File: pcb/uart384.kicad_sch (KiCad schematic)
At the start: 33 parts, among them IC1 ICE40LP384-SG32, J1 USB_A, J2 TC2050, J3 Conn_02x06_Odd_Even, SW1 SW_Push, U1 CP2102-QFN28, U2 AT25DF256-SSHN, U3 MIC5365-1.2YC5, Y1 XO32

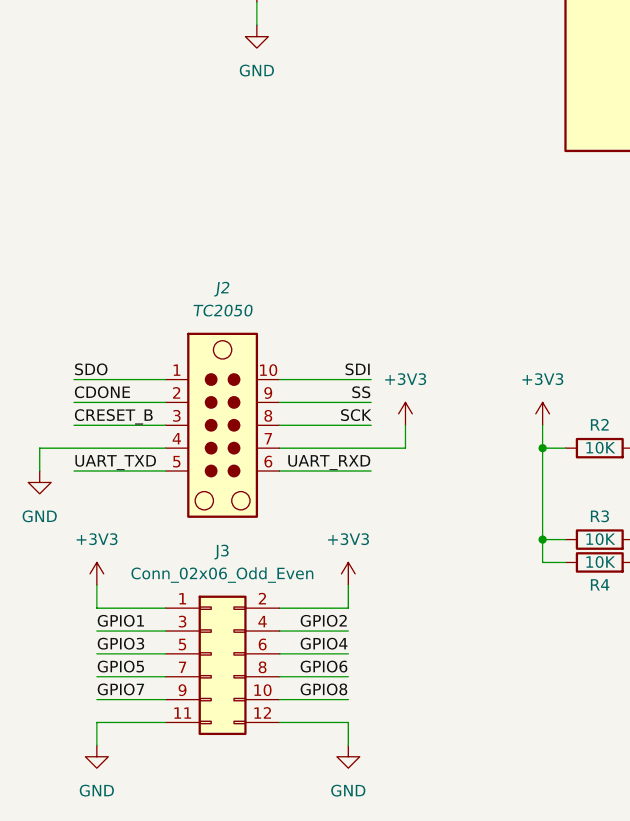
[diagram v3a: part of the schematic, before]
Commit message: PCB: add 5V to pinheader, move switch, LED, some resistors, improve routing
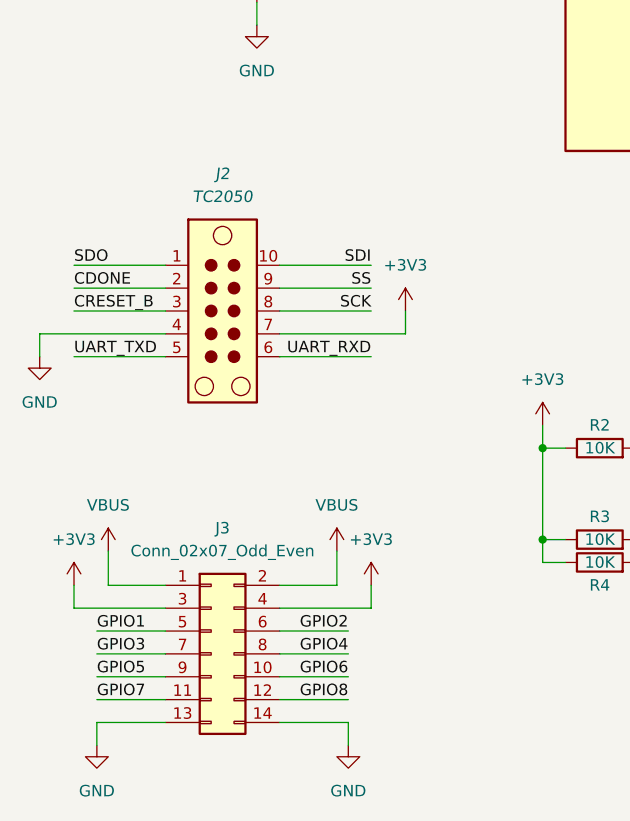
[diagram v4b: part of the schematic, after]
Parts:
- removed J3: Conn_02x06_Odd_Even, Connector_PinHeader_2.54mm:PinHeader_2x06_P2.54mm_Vertical, symbol Connector_Generic:Conn_02x06_Odd_Even
- added J3: Conn_02x07_Odd_Even, Connector_PinHeader_2.54mm:PinHeader_2x07_P2.54mm_Vertical, symbol Connector_Generic:Conn_02x07_Odd_Even
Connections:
- net +3V3: now also J3.3 (Pin_3), J3.4 (Pin_4)
- net GND: now also J3.13 (Pin_13), J3.14 (Pin_14)
- net GPIO1: now also J3.5 (Pin_5)
- net GPIO2: now also J3.6 (Pin_6)
- net GPIO3: now also J3.7 (Pin_7)
- net GPIO4: now also J3.8 (Pin_8)
- net GPIO5: now also J3.9 (Pin_9)
- net GPIO6: now also J3.10 (Pin_10)
- net GPIO7: now also J3.11 (Pin_11)
- net GPIO8: now also J3.12 (Pin_12)
- net VBUS: now also J3.1 (Pin_1), J3.2 (Pin_2)
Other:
- moved on the sheet: J2

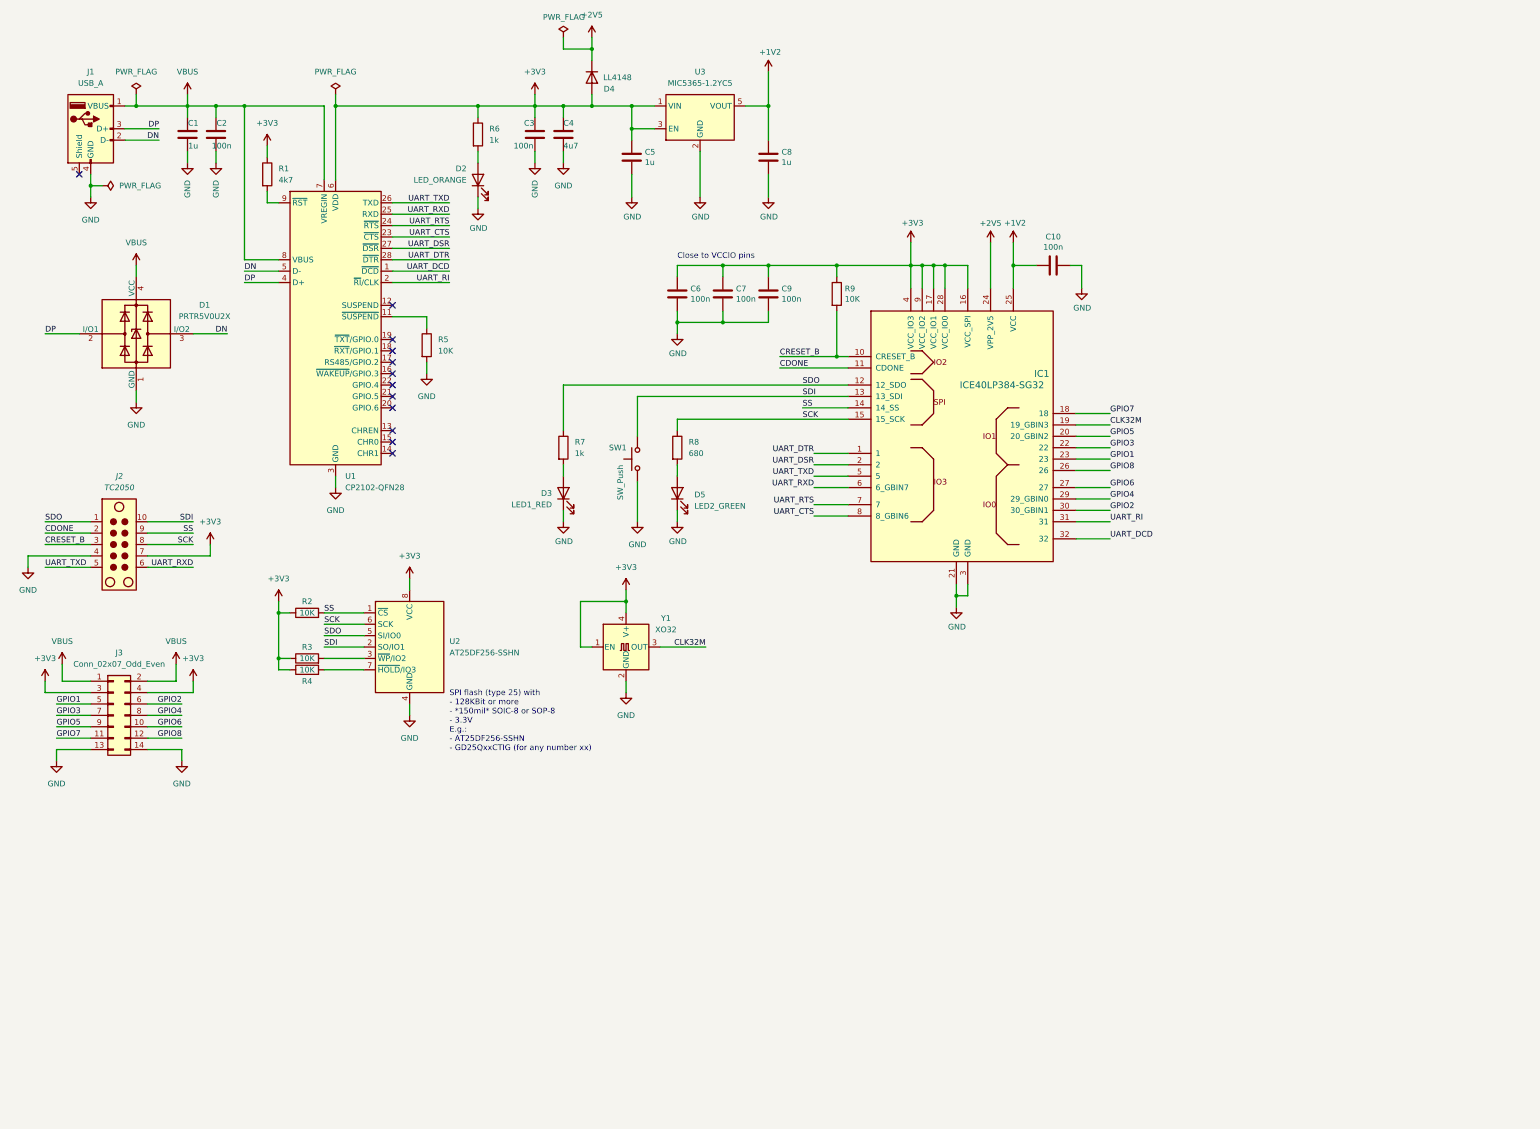
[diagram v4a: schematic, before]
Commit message: PCB: add additional header for upstream TC2050, re-route PCB.
Adding J4 for the "other" side of a TC2050 cable allows programming a
UART384 with another UART384, once a gateware is written that also can
control CDONE and CRESET lines. This enables full bootstrapping of a
UART384 with a UART384 :-D
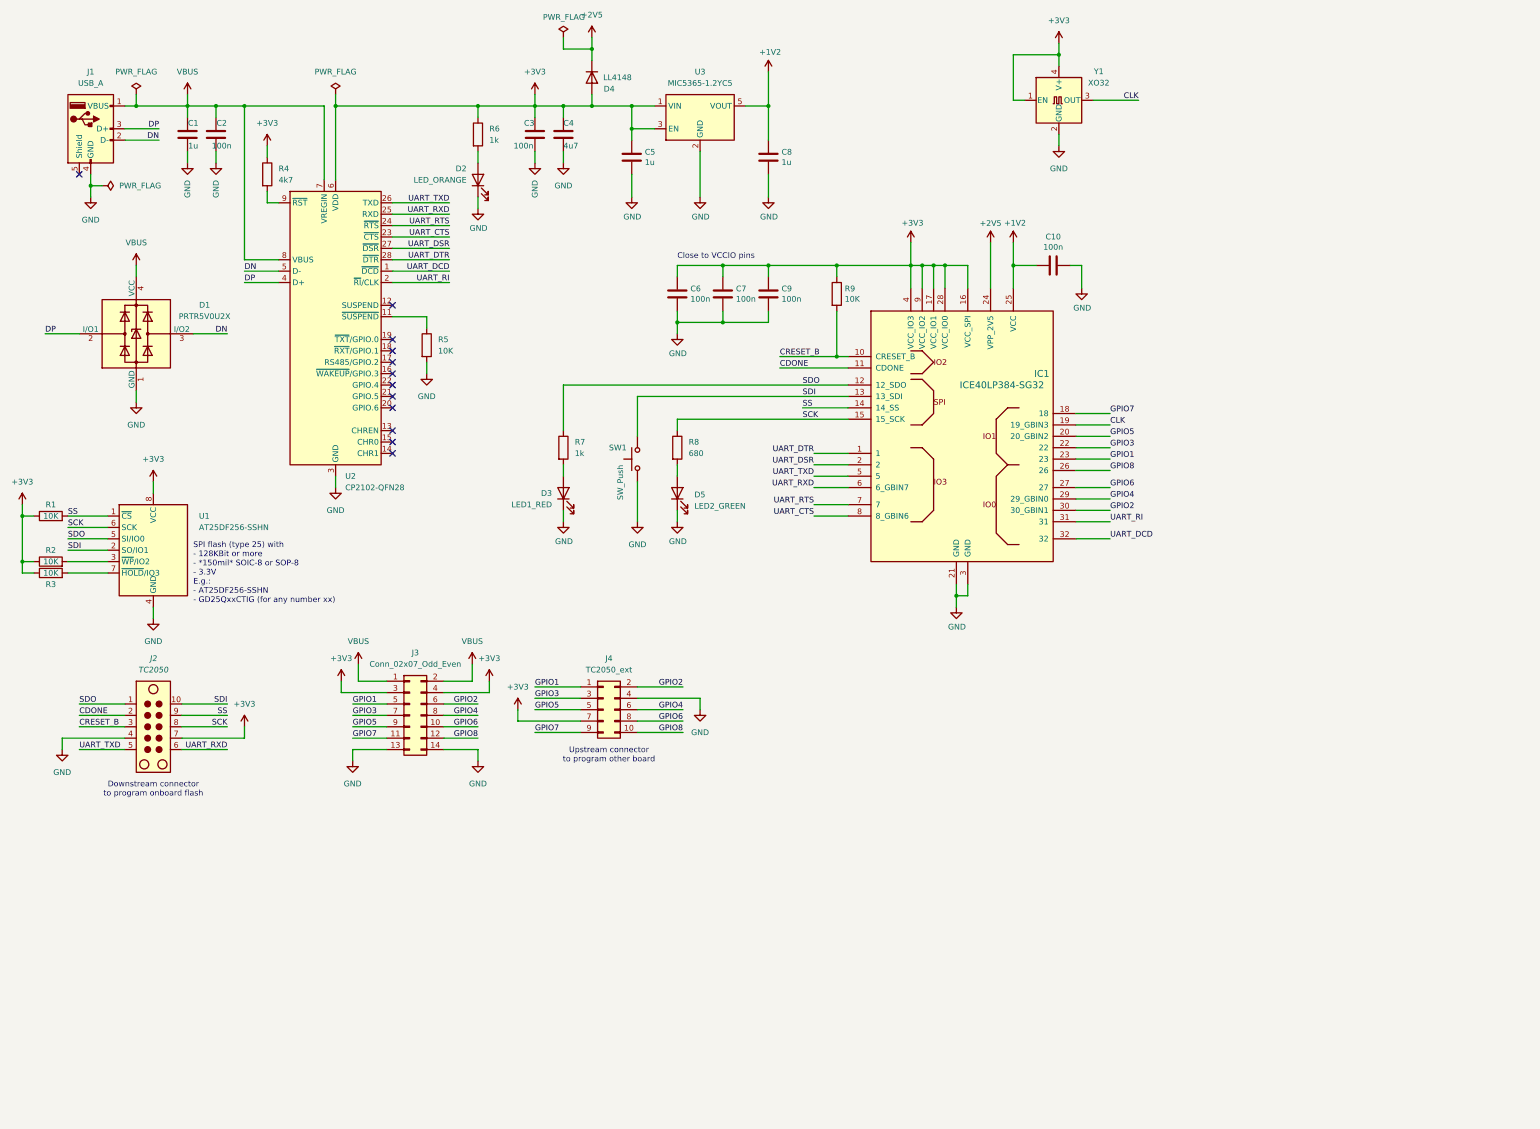
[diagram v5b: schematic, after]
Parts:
- added J4: TC2050_ext, Connector_PinHeader_2.54mm:PinHeader_2x05_P2.54mm_Vertical_SMD, symbol Connector_Generic:Conn_02x05_Odd_Even
- J3: footprint Connector_PinHeader_2.54mm:PinHeader_2x07_P2.54mm_Vertical -> Connector_PinHeader_2.54mm:PinHeader_2x07_P2.54mm_Vertical_SMD
- renumbered R2 to R1, R3 to R2, R4 to R3, R1 to R4, U2 to U1, U1 to U2
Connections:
- net +3V3: now also J4.7 (Pin_7)
- net GND: now also J4.4 (Pin_4)
- net GPIO1: now also J4.1 (Pin_1)
- net GPIO2: now also J4.2 (Pin_2)
- net GPIO3: now also J4.3 (Pin_3)
- net GPIO4: now also J4.6 (Pin_6)
- net GPIO5: now also J4.5 (Pin_5)
- net GPIO6: now also J4.8 (Pin_8)
- net GPIO7: now also J4.9 (Pin_9)
- net GPIO8: now also J4.10 (Pin_10)
- net CLK32M renamed CLK
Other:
- note added: "Downstream connector to program onboard flash"
- note added: "Upstream connector to program other board"
- moved on the sheet: J2, J3, R1, R2, R3, U1, Y1

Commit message: PCB: add LP384 GND center pad from upstream symbol, improve schematic and routing
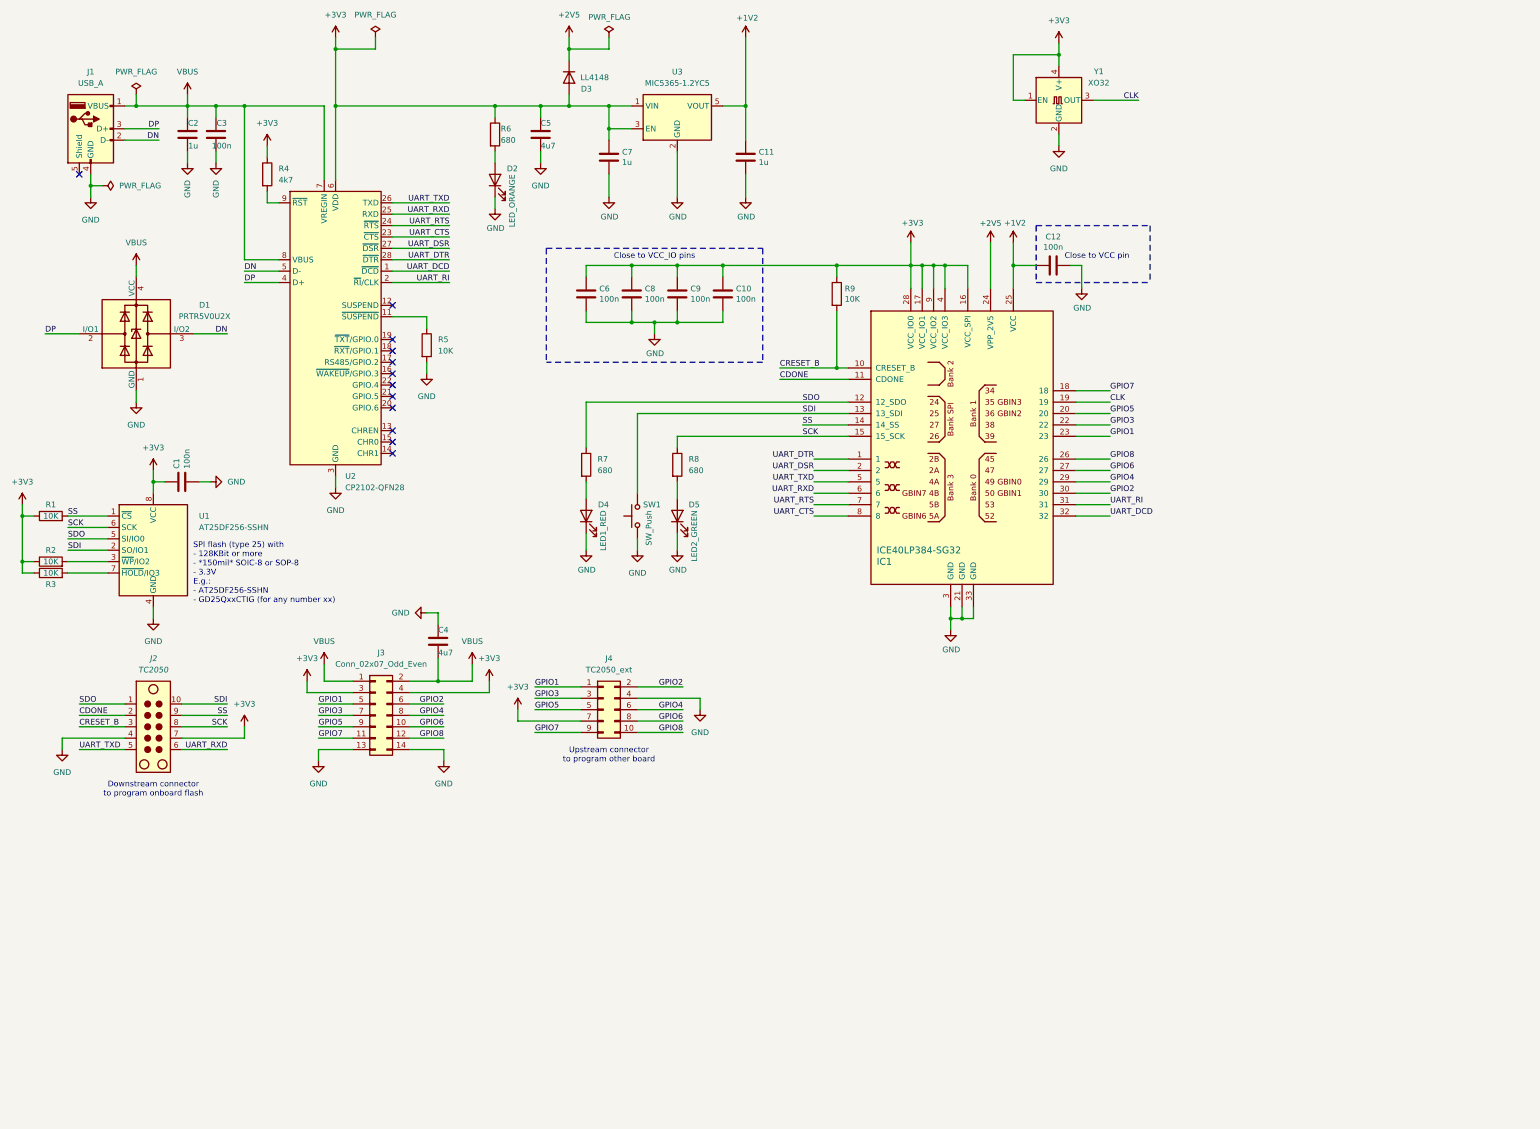
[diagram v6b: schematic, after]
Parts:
- removed C3: 100n, Capacitor_SMD:C_0603_1608Metric, symbol Device:C
- added C1, C6: 100n, Capacitor_SMD:C_0603_1608Metric, symbol Device:C
- added C4: 4u7, Capacitor_SMD:C_0603_1608Metric, symbol Device:C
- R6, R7: value 1k -> 680
- renumbered C9 to C10, C8 to C11, C10 to C12, C1 to C2, C2 to C3, C4 to C5, C5 to C7, C6 to C8, C7 to C9, D4 to D3, D3 to D4
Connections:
- net +3V3: now also C1.1, C6.1
- net GND: now also IC1.33 (GND), C1.2, C4.1, C6.2
- net VBUS: now also C4.2
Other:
- note added: "Close to VCC pin"
- note added: "Close to VCC_IO pins"
- note removed: "Close to VCCIO pins"
- moved on the sheet: C10, C11, C5, C7, C8, C9, D2, D3, D4, D5, J3, R6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

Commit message: PCB: major hardware revision 2.0~DEV: restructure FPGA pinout, fully reroute.
- re-map iCE40LP384 pins for GPIO 1-8, UART, CLK to optimize usability
  and allow experiments with LVDS pairs.

- allow voltage selection for LVDS pins (bank 3) between 3v3 (default)
  and 2v5 (untested, only via diode drop!).

- make programming pad TC2050 fully available, take care not to place
  components on other side of it.

- fully place&route, then optimization of PCB, planes etc.

- provide PCF files for both hardware revisions
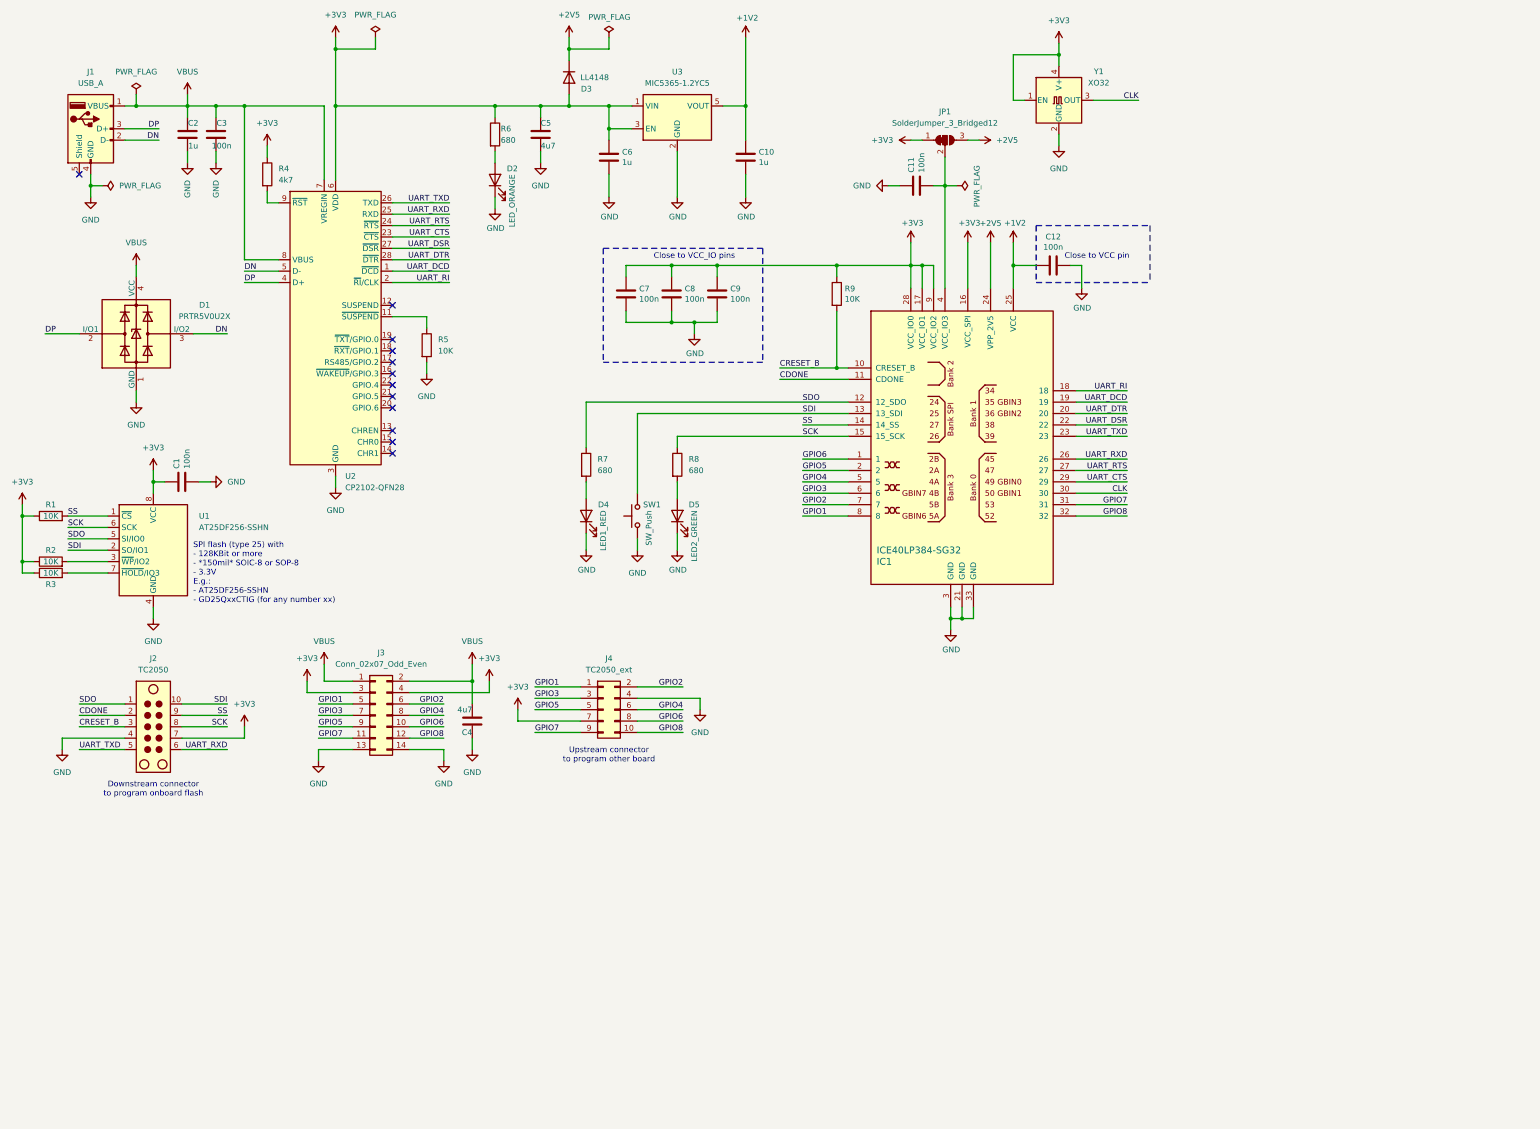
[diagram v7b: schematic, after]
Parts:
- added JP1: SolderJumper_3_Bridged12, Jumper:SolderJumper-3_P1.3mm_Bridged2Bar12_RoundedPad1.0x1.5mm, symbol Jumper:SolderJumper_3_Bridged12
- renumbered C11 to C10, C10 to C11, C7 to C6, C6 to C7
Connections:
- net +2V5: now also JP1.3 (B)
- net +3V3: now also JP1.1 (A); no longer C11.1, IC1.4 (VCC_IO3)
- net CLK: now also IC1.30; no longer IC1.19
- net GND: now also C11.1; no longer C11.2
- net GPIO1: now also IC1.8; no longer IC1.23
- net GPIO2: now also IC1.7; no longer IC1.30
- net GPIO3: now also IC1.6; no longer IC1.22
- net GPIO4: now also IC1.5; no longer IC1.29
- net GPIO5: now also IC1.2; no longer IC1.20
- net GPIO6: now also IC1.1; no longer IC1.27
- net GPIO7: now also IC1.31; no longer IC1.18
- net GPIO8: now also IC1.32; no longer IC1.26
- net UART_CTS: now also IC1.29; no longer IC1.8
- net UART_DCD: now also IC1.19; no longer IC1.32
- net UART_DSR: now also IC1.22; no longer IC1.2
- net UART_DTR: now also IC1.20; no longer IC1.1
- net UART_RI: now also IC1.18; no longer IC1.31
- net UART_RTS: now also IC1.27; no longer IC1.7
- net UART_RXD: now also IC1.26; no longer IC1.6
- net UART_TXD: now also IC1.23; no longer IC1.5
- new net: C11.2, IC1.4 (VCC_IO3), JP1.2 (C)
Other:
- moved on the sheet: C11, C4, C7, C8, C9
